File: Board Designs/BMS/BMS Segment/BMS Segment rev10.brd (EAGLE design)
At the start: 108 x 247.1 mm, 269 parts

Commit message: BMS segment rev10: silkscreen adjustments
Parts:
- C6_A, C6_B, C7_A, C7_B: value 0.1uF -> 100nF
- J: value Jumper -> 0R
- moved THERM1 159.9 mm to (51.1, 45.3)
- moved THERM4 159.9 mm to (51.1, 205.2)
- moved THERM2 53.2 mm to (51.1, 98.3)
- moved THERM3 53.2 mm to (51.1, 151.5)
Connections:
- net N$17: now also THERM1.2; no longer THERM4.2
- net N$19: now also THERM2.2; no longer THERM3.2
- net N$34: now also THERM4.2; no longer THERM1.2
- net N$36: now also THERM3.2; no longer THERM2.2
- net V-_A: now also THERM3.1, THERM4.1; no longer THERM1.1, THERM2.1
- net V-_B: now also THERM1.1, THERM2.1; no longer THERM3.1, THERM4.1
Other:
- board text added: "#"
- board text added: "HyTech 2018 BMS Segment rev10 Designed by Yvonne Yeh, based on rev7 by Brian Kaplan & Nathan Cheek"
- board text removed: "HyTech 2018 BMS Segment rev9 Designed by Yvonne Yeh, based on rev7 by Brian Kaplan & Nathan Cheek"

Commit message: BMS rev10: updated silkscreen and library footprints
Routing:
- net N$5: track 9.55 -> 10.7 mm
- net ISOSPI-P: track 52.8 -> 53.7 mm
- net CC10: track 28.0 -> 27.2 mm

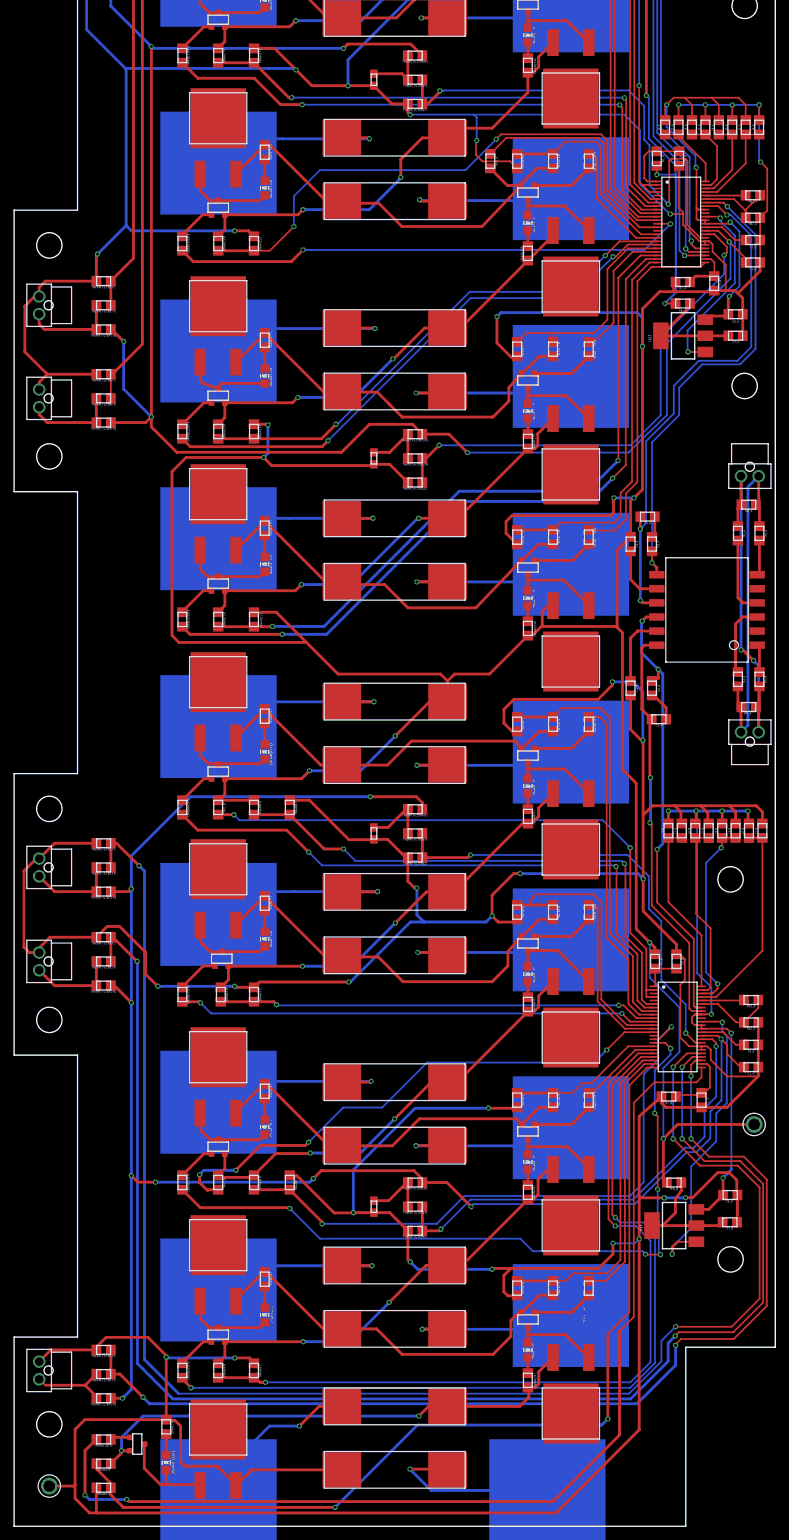
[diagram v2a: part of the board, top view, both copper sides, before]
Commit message: BMS rev10: make # box bigger, added and moved test points
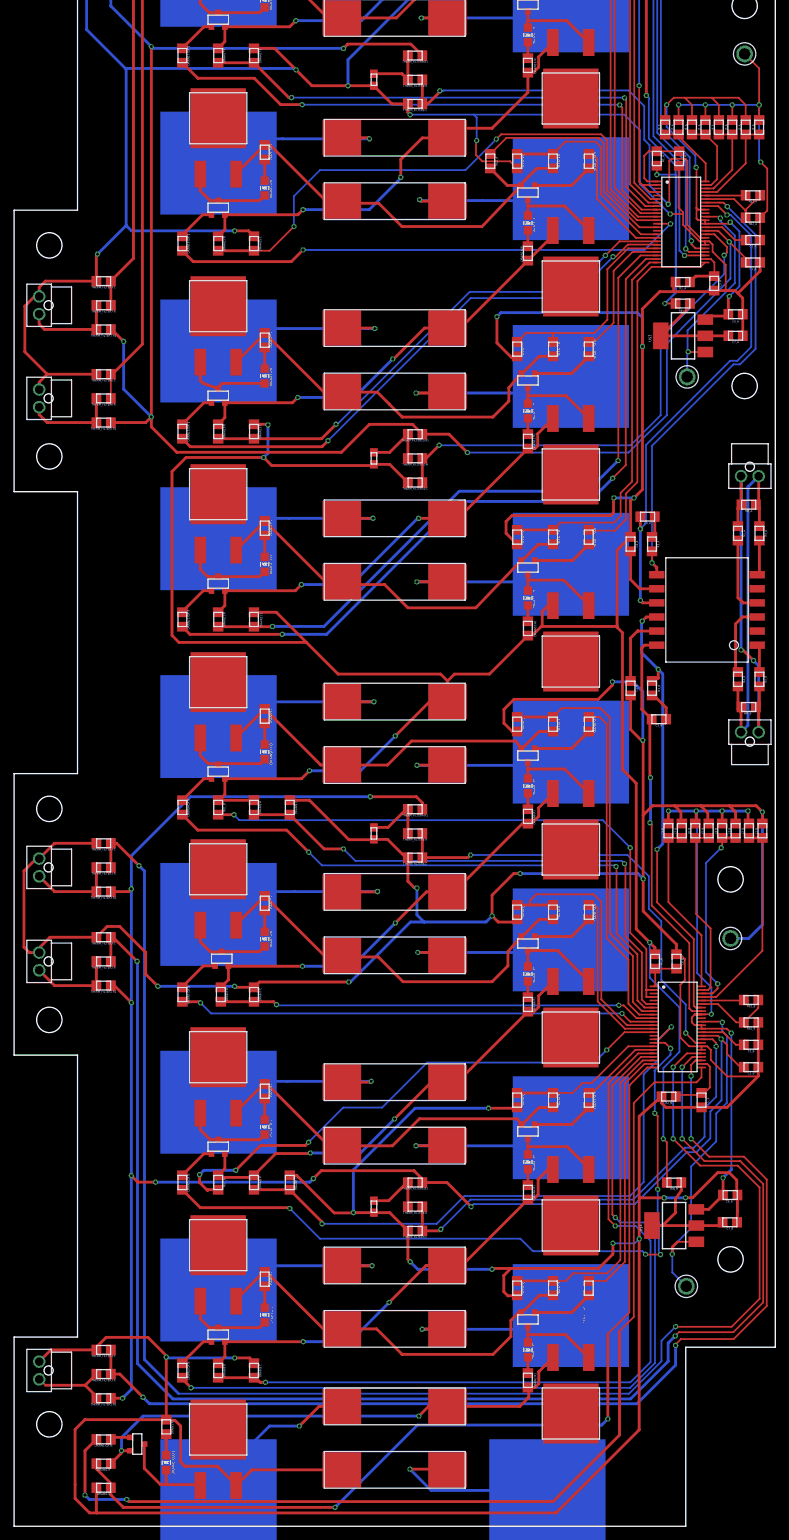
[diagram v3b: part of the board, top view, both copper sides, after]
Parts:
- added U$7, U$8: TEST_POINT, HyTechDevices:TEST_POINT
- moved U$5 151.9 mm to (103.7, 208.9)
- moved U$6 124.0 mm to (101.7, 83.4), turned to 90 degrees
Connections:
- net DRIVE_A: now also U$8.P$1
- net DRIVE_B: now also U$7.P$1
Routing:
- net V-_B: track 677.6 -> 695.2 mm, vias 19 -> 20
- net V-_A: track 791.0 -> 785.0 mm
- net DRIVE_B: track 44.1 -> 49.5 mm
- net DRIVE_A: track 27.3 -> 30.9 mm
- net IM_A: track 74.1 -> 71.5 mm
- net IP_A: track 68.4 -> 65.8 mm
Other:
- board text added: "DRIVE_A"
- board text added: "DRIVE_B"

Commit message: BMS Segment rev10: changed to smaller spring pads
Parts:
- moved CELL0 1.00 mm to (75.7, 6.04)
- moved CELL1 1.00 mm to (29.0, 6.04)
- moved CELL18 1.00 mm to (75.7, 239.9)
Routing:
- net CC18: track 29.6 -> 30.8 mm
- net CC1: track 23.6 -> 22.6 mm
- net CC0: track 26.2 -> 27.1 mm
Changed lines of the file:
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@@
 <setting verticaltext="up"/>
 </settings>
-<grid distance="5" unitdist="mil" unit="mil" style="lines" multiple="1" display="yes" altdistance="2" altunitdist="mil" altunit="mil"/>
+<grid distance="5" unitdist="mil" unit="mm" style="lines" multiple="1" display="yes" altdistance="2" altunitdist="mil" altunit="mm"/>
 <layers>
 <layer number="1" name="Top" color="4" fill="1" visible="yes" active="yes"/>
@@
 <layer number="20" name="Dimension" color="14" fill="1" visible="yes" active="yes"/>
 <layer number="21" name="tPlace" color="7" fill="1" visible="yes" active="yes"/>
-<layer number="22" name="bPlace" color="7" fill="1" visible="no" active="yes"/>
+<layer number="22" name="bPlace" color="7" fill="1" visible="yes" active="yes"/>
 <layer number="23" name="tOrigins" color="15" fill="1" visible="yes" active="yes"/>
-<layer number="24" name="bOrigins" color="15" fill="1" visible="no" active="yes"/>
+<layer number="24" name="bOrigins" color="15" fill="1" visible="yes" active="yes"/>
 <layer number="25" name="tNames" color="7" fill="1" visible="yes" active="yes"/>
-<layer number="26" name="bNames" color="7" fill="1" visible="no" active="yes"/>
+<layer number="26" name="bNames" color="7" fill="1" visible="yes" active="yes"/>
 <layer number="27" name="tValues" color="7" fill="1" visible="yes" active="yes"/>
-<layer number="28" name="bValues" color="7" fill="1" visible="no" active="yes"/>
+<layer number="28" name="bValues" color="7" fill="1" visible="yes" active="yes"/>
 <layer number="29" name="tStop" color="7" fill="3" visible="no" active="yes"/>
 <layer number="30" name="bStop" color="7" fill="6" visible="no" active="yes"/>
@@
 <layer number="38" name="bTest" color="7" fill="1" visible="no" active="yes"/>
 <layer number="39" name="tKeepout" color="4" fill="11" visible="yes" active="yes"/>
-<layer number="40" name="bKeepout" color="1" fill="11" visible="no" active="yes"/>
+<layer number="40" name="bKeepout" color="1" fill="11" visible="yes" active="yes"/>
 <layer number="41" name="tRestrict" color="4" fill="10" visible="yes" active="yes"/>
-<layer number="42" name="bRestrict" color="1" fill="10" visible="no" active="yes"/>
+<layer number="42" name="bRestrict" color="1" fill="10" visible="yes" active="yes"/>
 <layer number="43" name="vRestrict" color="2" fill="10" visible="no" active="yes"/>
-<layer number="44" name="Drills" color="7" fill="1" visible="no" active="yes"/>
+<layer number="44" name="Drills" color="7" fill="1" visible="yes" active="yes"/>
 <layer number="45" name="Holes" color="7" fill="1" visible="yes" active="yes"/>
 <layer number="46" name="Milling" color="3" fill="1" visible="no" active="yes"/>
 <layer number="47" name="Measures" color="7" fill="1" visible="no" active="yes"/>
 <layer number="48" name="Document" color="7" fill="1" visible="no" active="yes"/>
-<layer number="49" name="Reference" color="7" fill="1" visible="yes" active="yes"/>
+<layer number="49" name="Reference" color="7" fill="1" visible="no" active="yes"/>
 <layer number="50" name="dxf" color="7" fill="1" visible="no" active="no"/>
 <layer number="51" name="tDocu" color="7" fill="1" visible="yes" active="yes"/>
-<layer number="52" name="bDocu" color="7" fill="1" visible="no" active="yes"/>
+<layer number="52" name="bDocu" color="7" fill="1" visible="yes" active="yes"/>
 <layer number="53" name="tGND_GNDA" color="7" fill="9" visible="no" active="no"/>
 <layer number="54" name="bGND_GNDA" color="1" fill="9" visible="no" active="no"/>
@@
 <attribute name="NAME" x="83.82" y="29.89" size="1.778" layer="26" rot="MR270" align="top-center"/>
 </element>
-<element name="CELL1" library="HyTechDevices" package="KEYSTONE5222" value="BATTERY_SPRING_KEYSTONE5222" x="29" y="5.04" smashed="yes" rot="MR270">
-<attribute name="NAME" x="33.782" y="5.04" size="1.778" layer="26" rot="MR270" align="top-center"/>
+<element name="CELL1" library="HyTechDevices" package="KEYSTONE5222" value="BATTERY_SPRING_KEYSTONE5222" x="29" y="6.04" smashed="yes" rot="MR270">
+<attribute name="NAME" x="33.782" y="6.04" size="1.778" layer="26" rot="MR270" align="top-center"/>
 </element>
-<element name="CELL0" library="HyTechDevices" package="KEYSTONE5222" value="BATTERY_SPRING_KEYSTONE5222" x="75.66" y="5.04" smashed="yes" rot="MR270">
-<attribute name="NAME" x="80.518" y="5.04" size="1.778" layer="26" rot="MR270" align="top-center"/>
+<element name="CELL0" library="HyTechDevices" package="KEYSTONE5222" value="BATTERY_SPRING_KEYSTONE5222" x="75.66" y="6.04" smashed="yes" rot="MR270">
+<attribute name="NAME" x="80.518" y="6.04" size="1.778" layer="26" rot="MR270" align="top-center"/>
 </element>
 <element name="DRAIN1:GATE" library="HyTechDevices" package="0805" value="3K3" x="12.7" y="12.319" smashed="yes" rot="R180">
@@
 <element name="F11" library="HyTechDevices" package="5X20MM_FUSE" value="0001.2704.11" x="54" y="143" smashed="yes"/>
 <element name="F10" library="HyTechDevices" package="5X20MM_FUSE" value="0001.2704.11" x="54" y="134" smashed="yes" rot="R180"/>
-<element name="CELL18" library="HyTechDevices" package="KEYSTONE5222" value="BATTERY_SPRING_KEYSTONE5222" x="75.66" y="240.93" smashed="yes" rot="MR270">
-<attribute name="NAME" x="80.359" y="240.93" size="1.778" layer="26" rot="MR270" align="top-center"/>
+<element name="CELL18" library="HyTechDevices" package="KEYSTONE5222" value="BATTERY_SPRING_KEYSTONE5222" x="75.66" y="239.93" smashed="yes" rot="MR270">
+<attribute name="NAME" x="80.359" y="239.93" size="1.778" layer="26" rot="MR270" align="top-center"/>
 </element>
 <element name="CELL17" library="HyTechDevices" package="KEYSTONE5222" value="BATTERY_SPRING_KEYSTONE5222" x="29" y="220.05" smashed="yes" rot="MR270">
@@
 <wire x1="46.5" y1="17" x2="43.268775" y2="17" width="0.4064" layer="1"/>
 <wire x1="43.268775" y1="17" x2="40.480075" y2="14.2113" width="0.4064" layer="1"/>
-<wire x1="36.2409" y1="14.2113" x2="29" y2="6.9704" width="0.4064" layer="16"/>
-<wire x1="29" y1="5.04" x2="29" y2="6.9704" width="0.4064" layer="16"/>
+<wire x1="36.2409" y1="14.2113" x2="29.3663" y2="7.3367" width="0.4064" layer="16"/>
 <wire x1="36.2409" y1="14.2113" x2="40.480075" y2="14.2113" width="0.4064" layer="16"/>
+<wire x1="29" y1="6.04" x2="29" y2="6.9704" width="0.4064" layer="16"/>
+<wire x1="29" y1="6.9704" x2="29.3663" y2="7.3367" width="0.4064" layer="16"/>
 </signal>
 <signal name="CC0" class="1">
@@
 <wire x1="56.1594" y1="8.1026" x2="61.3974" y2="8.1026" width="0.4064" layer="1"/>
 <wire x1="61.3974" y1="8.1026" x2="61.5" y2="8" width="0.4064" layer="1"/>
-<wire x1="75.66" y1="5.04" x2="75.62" y2="5.08" width="0.4064" layer="16"/>
+<wire x1="75.66" y1="6.04" x2="75.62" y2="5.08" width="0.4064" layer="16"/>
 <wire x1="75.62" y1="5.08" x2="59.182" y2="5.08" width="0.4064" layer="16"/>
 </signal>
@@
 <wire x1="53.9096" y1="240.48" x2="53.8656" y2="240.524" width="0.4064" layer="1"/>
 <wire x1="53.8796" y1="240.538" x2="53.8656" y2="240.524" width="0.4064" layer="16"/>
-<wire x1="75.66" y1="240.93" x2="75.268" y2="240.538" width="0.4064" layer="16"/>
-<wire x1="75.268" y1="240.538" x2="53.8796" y2="240.538" width="0.4064" layer="16"/>
+<wire x1="75.268" y1="240.538" x2="74.549" y2="240.538" width="0.4064" layer="16"/>
+<wire x1="74.549" y1="240.538" x2="53.8796" y2="240.538" width="0.4064" layer="16"/>
+<wire x1="75.66" y1="239.93" x2="74.941" y2="240.93" width="0.4064" layer="16"/>
+<wire x1="74.941" y1="240.93" x2="74.549" y2="240.538" width="0.4064" layer="16"/>
 </signal>
 <signal name="CC17" class="1">

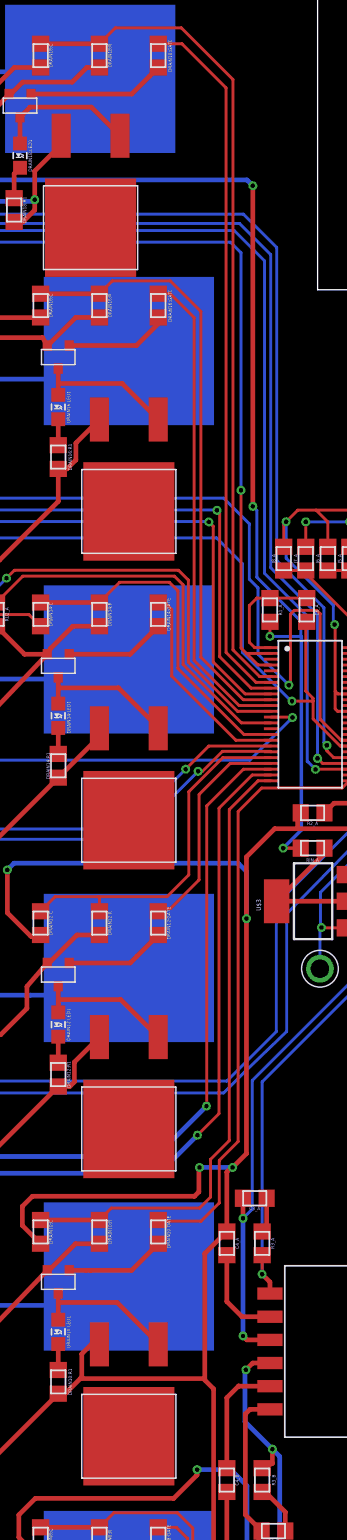
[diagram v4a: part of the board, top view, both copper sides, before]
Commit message: Main ECU: tweak trace location, BMS: adjust silkscreen for manufacturing
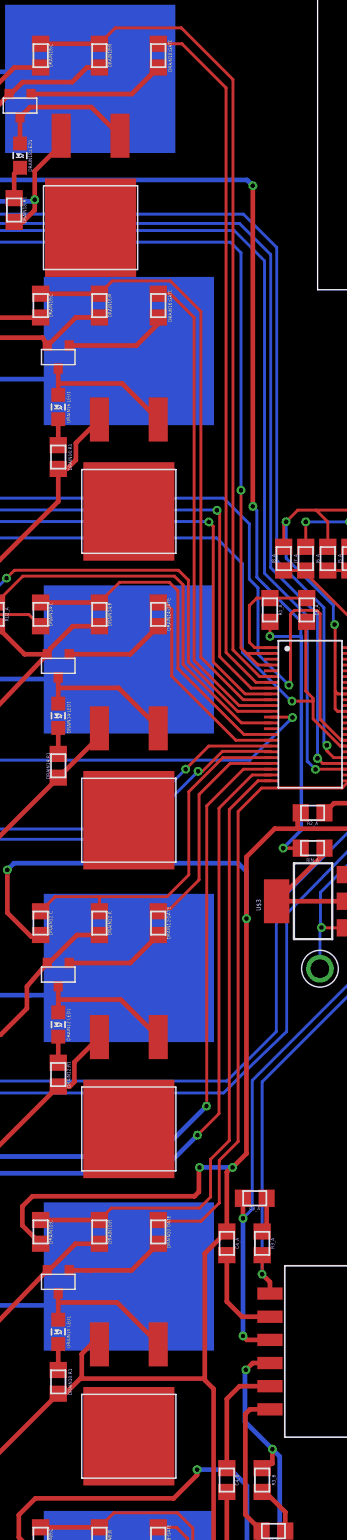
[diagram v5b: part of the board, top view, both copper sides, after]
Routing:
- net CC18: track 30.8 -> 30.1 mm
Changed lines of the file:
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@@
 <setting verticaltext="up"/>
 </settings>
-<grid distance="5" unitdist="mil" unit="mm" style="lines" multiple="1" display="yes" altdistance="2" altunitdist="mil" altunit="mm"/>
+<grid distance="0.1" unitdist="mm" unit="mm" style="lines" multiple="1" display="yes" altdistance="2" altunitdist="mil" altunit="mm"/>
 <layers>
 <layer number="1" name="Top" color="4" fill="1" visible="yes" active="yes"/>
@@
 <wire x1="83.312" y1="1.016" x2="83.312" y2="10.414" width="0.4064" layer="51"/>
 <wire x1="83.312" y1="10.414" x2="65.405" y2="10.414" width="0.4064" layer="51"/>
-<text x="68.834" y="5.588" size="6.35" layer="51" font="vector" align="center">#</text>
+<text x="68.76" y="5.588" size="6.35" layer="51" font="vector" align="center">#</text>
 <rectangle x1="70.485" y1="1.016" x2="83.312" y2="10.414" layer="51"/>
 <text x="97.79" y="34.036" size="1.016" layer="51" font="vector" rot="R270" align="center">DRIVE_B</text>
@@
 <element name="ISOSPI_B" library="HyTechDevices" package="NANO-FIT_VERTICAL-2" value="CONNECTOR-2NANO-FIT_VERTICAL-2" x="104.394" y="112.662" smashed="yes"/>
 <element name="THERM2" library="HyTechDevices" package="0603" value="10K" x="51.054" y="98.298" smashed="yes" rot="R90">
-<attribute name="NAME" x="52.7431" y="98.298" size="1.016" layer="27" font="vector" rot="R90" align="bottom-center"/>
+<attribute name="NAME" x="51.8569" y="98.302" size="1.016" layer="27" font="vector" rot="R270" align="bottom-center"/>
 <attribute name="VALUE" x="50.2412" y="98.298" size="1.016" layer="27" font="vector" rot="R90" align="bottom-center"/>
 </element>
 <element name="THERM1" library="HyTechDevices" package="0603" value="10K" x="51.054" y="45.339" smashed="yes" rot="R90">
-<attribute name="NAME" x="52.7431" y="45.339" size="1.016" layer="27" font="vector" rot="R90" align="bottom-center"/>
-<attribute name="VALUE" x="49.4792" y="45.339" size="1.016" layer="27" font="vector" rot="R90" align="top-center"/>
+<attribute name="NAME" x="51.8569" y="45.361" size="1.016" layer="27" font="vector" rot="R270" align="bottom-center"/>
+<attribute name="VALUE" x="50.3208" y="45.361" size="1.016" layer="27" font="vector" rot="R270" align="top-center"/>
 </element>
 <element name="DRAIN1:R" library="HyTechDevices" package="0805" value="100R" x="12.7" y="8.89" smashed="yes" rot="R180">
@@
 <element name="ISOSPI_A" library="HyTechDevices" package="NANO-FIT_VERTICAL-2" value="CONNECTOR-2NANO-FIT_VERTICAL-2" x="104.394" y="148.984" smashed="yes" rot="R180"/>
 <element name="THERM4" library="HyTechDevices" package="0603" value="10K" x="51.054" y="205.232" smashed="yes" rot="R90">
-<attribute name="NAME" x="52.7431" y="205.232" size="1.016" layer="27" font="vector" rot="R90" align="bottom-center"/>
+<attribute name="NAME" x="51.8569" y="205.268" size="1.016" layer="27" font="vector" rot="R270" align="bottom-center"/>
 <attribute name="VALUE" x="49.7332" y="205.232" size="1.016" layer="27" font="vector" rot="R90" align="center"/>
 </element>
 <element name="THERM3" library="HyTechDevices" package="0603" value="10K" x="51.054" y="151.511" smashed="yes" rot="R90">
-<attribute name="NAME" x="52.6161" y="151.511" size="1.016" layer="27" font="vector" rot="R90" align="bottom-center"/>
-<attribute name="VALUE" x="50.2158" y="151.511" size="1.016" layer="27" font="vector" rot="R270" align="top-center"/>
+<attribute name="NAME" x="51.7839" y="151.489" size="1.016" layer="27" font="vector" rot="R270" align="bottom-center"/>
+<attribute name="VALUE" x="50.3158" y="151.511" size="1.016" layer="27" font="vector" rot="R270" align="top-center"/>
 </element>
 <element name="R2_A" library="HyTechDevices" package="0805" value="100R" x="94.869" y="176.53" smashed="yes">
@@
 <contactref element="C4_B" pad="1"/>
 <contactref element="TRANSFORMER" pad="P$11"/>
-<wire x1="88.476" y1="127.027" x2="87.46" y2="126.011" width="0.4064" layer="1"/>
-<wire x1="87.46" y1="119.924" x2="87.46" y2="126.011" width="0.4064" layer="1"/>
-<wire x1="91.1854" y1="127.0064" x2="88.4966" y2="127.0064" width="0.4064" layer="1"/>
-<wire x1="88.4966" y1="127.0064" x2="88.476" y2="127.027" width="0.4064" layer="1"/>
+<wire x1="88.5554" y1="127.0064" x2="87.46" y2="125.911" width="0.4064" layer="1"/>
+<wire x1="87.46" y1="119.924" x2="87.46" y2="125.911" width="0.4064" layer="1"/>
+<wire x1="91.1854" y1="127.0064" x2="88.5554" y2="127.0064" width="0.4064" layer="1"/>
 </signal>
 <signal name="N$5">
@@
 <wire x1="53.9096" y1="240.48" x2="53.8656" y2="240.524" width="0.4064" layer="1"/>
 <wire x1="53.8796" y1="240.538" x2="53.8656" y2="240.524" width="0.4064" layer="16"/>
-<wire x1="75.268" y1="240.538" x2="74.549" y2="240.538" width="0.4064" layer="16"/>
 <wire x1="74.549" y1="240.538" x2="53.8796" y2="240.538" width="0.4064" layer="16"/>
 <wire x1="75.66" y1="239.93" x2="74.941" y2="240.93" width="0.4064" layer="16"/>
